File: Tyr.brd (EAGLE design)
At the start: 152.4 x 115.6 mm, 206 parts, among them J1 TYR_TYR_DISPLAY, Q1 DTC123J, SW1 BUTTON, U1 MCP1700T, U2 CONTROLLER_PRTR5V0U2X, U3 STM32F303CC, U4 MB85RC256V, U6 TYR_TPS2552, X1 CONTROLLER_USB-C-12PUSB-C-12P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, Y1 8Mhz

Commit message: Y branching
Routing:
- net 3.3V: track 397.3 -> 396.4 mm
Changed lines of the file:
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@@
 <wire x1="146.0921875" y1="69.74125" x2="145.4071875" y2="69.05625" width="0.3048" layer="16"/>
 <wire x1="151.209375" y1="31.5515625" x2="149.4234375" y2="31.5515625" width="0.3048" layer="16"/>
-<wire x1="149.4234375" y1="31.5515625" x2="147.6375" y2="31.5515625" width="0.3048" layer="16"/>
-<wire x1="147.6375" y1="31.5515625" x2="145.8515625" y2="31.5515625" width="0.3048" layer="16"/>
-<wire x1="145.8515625" y1="31.5515625" x2="144.065625" y2="31.5515625" width="0.3048" layer="16"/>
-<wire x1="144.065625" y1="31.5515625" x2="142.2796875" y2="31.5515625" width="0.3048" layer="16"/>
-<wire x1="142.2796875" y1="31.5515625" x2="140.49375" y2="31.5515625" width="0.3048" layer="16"/>
+<wire x1="148.828125" y1="31.5515625" x2="147.6375" y2="31.5515625" width="0.3048" layer="16"/>
+<wire x1="147.0421875" y1="31.5515625" x2="145.8515625" y2="31.5515625" width="0.3048" layer="16"/>
+<wire x1="145.25625" y1="31.5515625" x2="144.065625" y2="31.5515625" width="0.3048" layer="16"/>
+<wire x1="143.4703125" y1="31.5515625" x2="142.2796875" y2="31.5515625" width="0.3048" layer="16"/>
+<wire x1="141.684375" y1="31.5515625" x2="140.49375" y2="31.5515625" width="0.3048" layer="16"/>
 <wire x1="140.49375" y1="31.5515625" x2="140.19609375" y2="31.25390625" width="0.3048" layer="16"/>
 <wire x1="140.19609375" y1="31.25390625" x2="140.19609375" y2="30.6765625" width="0.3048" layer="16"/>
-<wire x1="141.98203125" y1="30.6765625" x2="141.98203125" y2="31.25390625" width="0.3048" layer="16"/>
 <wire x1="141.98203125" y1="31.25390625" x2="142.2796875" y2="31.5515625" width="0.3048" layer="16"/>
-<wire x1="143.76796875" y1="30.6765625" x2="143.76796875" y2="31.25390625" width="0.3048" layer="16"/>
 <wire x1="143.76796875" y1="31.25390625" x2="144.065625" y2="31.5515625" width="0.3048" layer="16"/>
-<wire x1="145.55390625" y1="30.6765625" x2="145.55390625" y2="31.25390625" width="0.3048" layer="16"/>
 <wire x1="145.55390625" y1="31.25390625" x2="145.8515625" y2="31.5515625" width="0.3048" layer="16"/>
-<wire x1="147.33984375" y1="30.6765625" x2="147.33984375" y2="31.25390625" width="0.3048" layer="16"/>
 <wire x1="147.33984375" y1="31.25390625" x2="147.6375" y2="31.5515625" width="0.3048" layer="16"/>
-<wire x1="149.12578125" y1="30.6765625" x2="149.12578125" y2="31.25390625" width="0.3048" layer="16"/>
 <wire x1="149.12578125" y1="31.25390625" x2="149.4234375" y2="31.5515625" width="0.3048" layer="16"/>
 <wire x1="147.33984375" y1="30.6765625" x2="149.12578125" y2="30.6765625" width="0.3048" layer="16"/>
@@
 <wire x1="118.4671875" y1="7.7390625" x2="115.8875" y2="10.31875" width="0.1524" layer="1"/>
 <wire x1="115.8875" y1="10.31875" x2="115.8875" y2="10.4775" width="0.1524" layer="1"/>
+<wire x1="148.828125" y1="31.5515625" x2="149.12578125" y2="31.25390625" width="0.3048" layer="16"/>
+<wire x1="149.12578125" y1="31.25390625" x2="149.12578125" y2="30.6765625" width="0.3048" layer="16"/>
+<wire x1="147.0421875" y1="31.5515625" x2="147.33984375" y2="31.25390625" width="0.3048" layer="16"/>
+<wire x1="147.33984375" y1="31.25390625" x2="147.33984375" y2="30.6765625" width="0.3048" layer="16"/>
+<wire x1="145.25625" y1="31.5515625" x2="145.55390625" y2="31.25390625" width="0.3048" layer="16"/>
+<wire x1="145.55390625" y1="31.25390625" x2="145.55390625" y2="30.6765625" width="0.3048" layer="16"/>
+<wire x1="143.4703125" y1="31.5515625" x2="143.76796875" y2="31.25390625" width="0.3048" layer="16"/>
+<wire x1="143.76796875" y1="31.25390625" x2="143.76796875" y2="30.6765625" width="0.3048" layer="16"/>
+<wire x1="141.684375" y1="31.5515625" x2="141.98203125" y2="31.25390625" width="0.3048" layer="16"/>
+<wire x1="141.98203125" y1="31.25390625" x2="141.98203125" y2="30.6765625" width="0.3048" layer="16"/>
 </signal>
 <signal name="NRST">

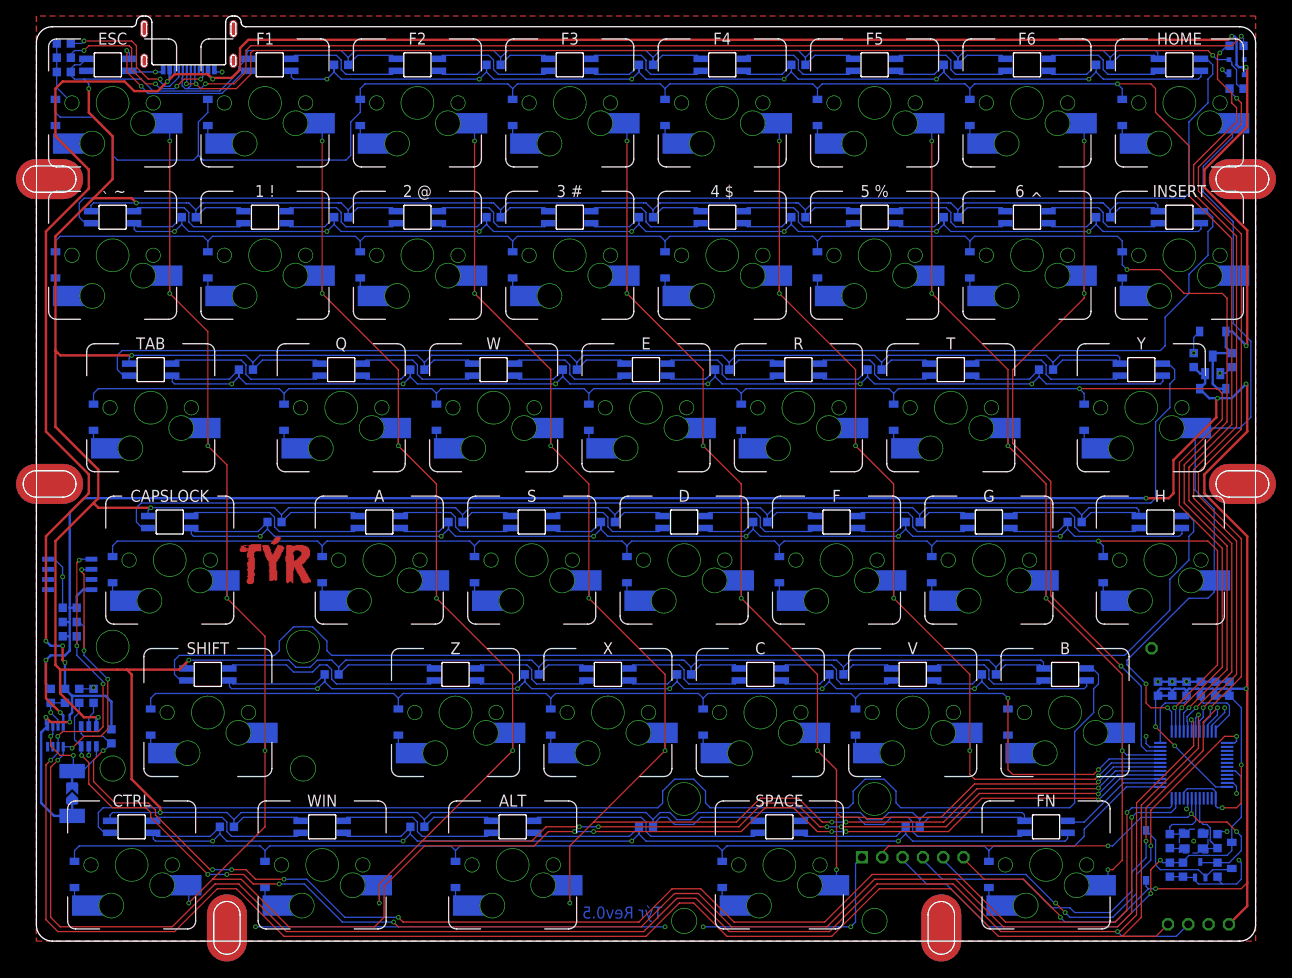
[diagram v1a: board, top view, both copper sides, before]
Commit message: Ground plane under STM32
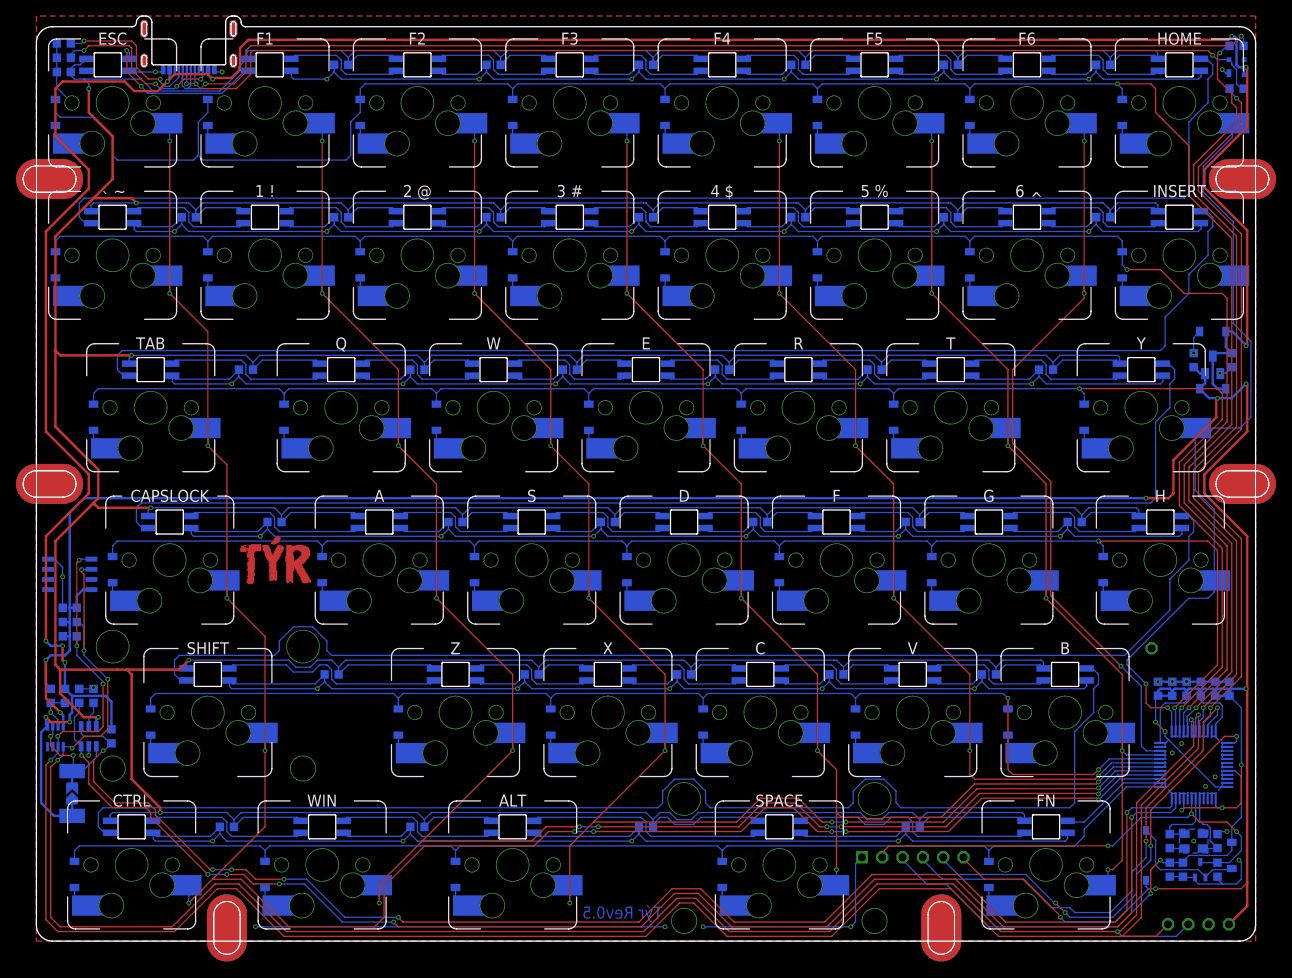
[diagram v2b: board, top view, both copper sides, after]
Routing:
- net GND: track 1189.0 -> 1175.5 mm
- net 3.3V: track 396.4 -> 396.0 mm, vias 12 -> 13

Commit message: Y branching
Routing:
- net LED_VCC: track 1250.6 -> 1226.3 mm

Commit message: Update logo
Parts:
- added U$1: LOGO_TYR, Tyr:LOGO_TYR_COPPER
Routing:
- net GND: track 1175.5 -> 1177.3 mm, vias 57 -> 59
- net COLUMN7: track 108.6 -> 107.8 mm
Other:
- board text added: "C:/Users/Brian/Desktop/TYR STOP.bmp"
- board text added: "C:/Users/Brian/Desktop/TYR TEXT.bmp"
- board text removed: "C:/Users/Brian/Desktop/Tyr V4.bmp"
- board text removed: "D:/Users/Brian/Pictures/Tyr.bmp"

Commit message: Update
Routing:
- net COLUMN7: track 107.8 -> 101.0 mm
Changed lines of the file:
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@@
 <text x="105.7275" y="8.5725" size="1" layer="22" font="vector" ratio="13" rot="MR315" align="center-left">NRST</text>
 <text x="103.1875" y="12.7" size="1" layer="22" font="vector" ratio="13" rot="MR0" align="center">GND</text>
-<text x="73.2234375" y="3.571875" size="1.5" layer="16" font="vector" ratio="13" rot="MR0" align="center">Týr Rev0.5</text>
-<text x="73.2234375" y="3.571875" size="1.5" layer="30" font="vector" ratio="13" rot="MR0" align="center">Týr Rev0.5</text>
+<text x="76.2" y="7.14375" size="1.5" layer="16" font="vector" ratio="13" rot="MR0" align="center">Týr Rev0.5</text>
+<text x="76.2" y="7.14375" size="1.5" layer="30" font="vector" ratio="13" rot="MR0" align="center">Týr Rev0.5</text>
 <text x="0" y="-0.5" size="0.2" layer="200" font="vector">C:/Users/Brian/Desktop/TYR TEXT.bmp</text>
 <text x="0" y="-0.5" size="0.2" layer="225" font="vector">C:/Users/Brian/Desktop/TYR STOP.bmp</text>
@@
 <contactref element="KEYSWITCH30" pad="P$1"/>
 <contactref element="KEYSWITCH23" pad="P$1"/>
-<wire x1="144.065625" y1="42.8625" x2="136.3265625" y2="35.1234375" width="0.1524" layer="16"/>
 <wire x1="145.8515625" y1="96.8446875" x2="145.8515625" y2="93.6553125" width="0.1524" layer="16"/>
 <wire x1="145.8515625" y1="93.6553125" x2="149.61" y2="89.896875" width="0.1524" layer="16"/>
@@
 <contactref element="KEYSWITCH30" pad="HOLE3"/>
 <wire x1="149.5190625" y1="100.5121875" x2="145.8515625" y2="96.8446875" width="0.1524" layer="16"/>
-<wire x1="144.065625" y1="42.8625" x2="146.446875" y2="42.8625" width="0.1524" layer="16"/>
-<wire x1="146.446875" y1="42.8625" x2="147.22875" y2="43.644375" width="0.1524" layer="16"/>
-<wire x1="147.22875" y1="43.644375" x2="147.22875" y2="45.085" width="0.1524" layer="16"/>
+<wire x1="147.0421875" y1="42.8625" x2="147.22875" y2="43.0490625" width="0.1524" layer="16"/>
+<wire x1="147.22875" y1="43.0490625" x2="147.22875" y2="45.085" width="0.1524" layer="16"/>
 <wire x1="149.5190625" y1="100.5121875" x2="149.5190625" y2="102.1440625" width="0.1524" layer="16"/>
 <wire x1="149.5190625" y1="102.1440625" x2="149.61" y2="102.235" width="0.1524" layer="16"/>
@@
 <wire x1="141.9109375" y1="26.2048625" x2="141.9109375" y2="28.64609375" width="0.1524" layer="16"/>
 <via x="141.38671875" y="29.1703125" extent="1-16" drill="0.35"/>
-<wire x1="141.38671875" y1="29.1703125" x2="139.303125" y2="29.1703125" width="0.1524" layer="1"/>
-<wire x1="139.303125" y1="29.1703125" x2="138.7078125" y2="29.765625" width="0.1524" layer="1"/>
-<wire x1="138.7078125" y1="29.765625" x2="138.7078125" y2="32.146875" width="0.1524" layer="1"/>
-<via x="138.7078125" y="32.146875" extent="1-16" drill="0.35"/>
-<wire x1="136.3265625" y1="35.1234375" x2="136.3265625" y2="34.528125" width="0.1524" layer="16"/>
-<wire x1="136.3265625" y1="34.528125" x2="138.7078125" y2="32.146875" width="0.1524" layer="16"/>
+<wire x1="141.38671875" y1="29.1703125" x2="147.0421875" y2="34.82578125" width="0.1524" layer="1"/>
+<wire x1="147.0421875" y1="34.82578125" x2="147.0421875" y2="42.8625" width="0.1524" layer="1"/>
+<via x="147.0421875" y="42.8625" extent="1-16" drill="0.35"/>
 </signal>
 <signal name="COLUMN6">
@@
 <wire x1="151.209375" y1="69.6515625" x2="149.4234375" y2="67.865625" width="0.3048" layer="16"/>
 <via x="151.209375" y="69.6515625" extent="1-16" drill="0.35"/>
-<via x="151.209375" y="31.5515625" extent="1-16" drill="0.35"/>
 <contactref element="J1" pad="VIN"/>
-<wire x1="151.358203125" y1="4.391953125" x2="151.358203125" y2="7.14375" width="0.3048" layer="1"/>
-<wire x1="151.358203125" y1="7.14375" x2="151.358203125" y2="7.292578125" width="0.3048" layer="1"/>
+<wire x1="151.358203125" y1="4.391953125" x2="151.358203125" y2="7.292578125" width="0.3048" layer="1"/>
 <wire x1="151.358203125" y1="4.391953125" x2="149.06625" y2="2.1" width="0.3048" layer="1"/>
 <via x="139.8984375" y="6.5484375" extent="1-16" drill="0.35"/>
 <wire x1="139.8984375" y1="6.5484375" x2="150.6140625" y2="6.5484375" width="0.1524" layer="1"/>
-<wire x1="151.358203125" y1="7.292578125" x2="151.209375" y2="7.14375" width="0.1524" layer="1"/>
 <contactref element="SW1" pad="P$2"/>
-<wire x1="151.209375" y1="7.14375" x2="150.6140625" y2="6.5484375" width="0.1524" layer="1"/>
+<wire x1="151.358203125" y1="7.292578125" x2="150.6140625" y2="6.5484375" width="0.1524" layer="1"/>
 <wire x1="139.8984375" y1="6.5484375" x2="139.005078125" y2="6.5484375" width="0.1524" layer="16"/>
 <contactref element="PH1" pad="6"/>
@@
 <wire x1="146.0921875" y1="70.9328125" x2="146.0921875" y2="69.74125" width="0.3048" layer="16"/>
 <wire x1="146.0921875" y1="69.74125" x2="145.4071875" y2="69.05625" width="0.3048" layer="16"/>
-<wire x1="151.209375" y1="31.5515625" x2="149.4234375" y2="31.5515625" width="0.3048" layer="16"/>
 <wire x1="148.828125" y1="31.5515625" x2="147.6375" y2="31.5515625" width="0.3048" layer="16"/>
 <wire x1="147.0421875" y1="31.5515625" x2="145.8515625" y2="31.5515625" width="0.3048" layer="16"/>
@@
 <wire x1="5.0421875" y1="43.1421875" x2="5.0421875" y2="41.671875" width="0.3048" layer="16"/>
 <wire x1="5.8340625" y1="43.9340625" x2="5.0421875" y2="43.1421875" width="0.3048" layer="16"/>
-<wire x1="151.358203125" y1="31.5515625" x2="151.358203125" y2="7.292578125" width="0.3048" layer="1"/>
-<wire x1="151.358203125" y1="31.5515625" x2="151.358203125" y2="50.6015625" width="0.3048" layer="1"/>
-<wire x1="151.209375" y1="31.5515625" x2="151.358203125" y2="31.5515625" width="0.3048" layer="1"/>
+<wire x1="151.358203125" y1="50.6015625" x2="151.358203125" y2="32.146875" width="0.3048" layer="1"/>
+<wire x1="151.358203125" y1="30.95625" x2="151.358203125" y2="7.292578125" width="0.3048" layer="1"/>
 <wire x1="118.4671875" y1="7.7390625" x2="115.8875" y2="10.31875" width="0.1524" layer="1"/>
 <wire x1="115.8875" y1="10.31875" x2="115.8875" y2="10.4775" width="0.1524" layer="1"/>
@@
 <wire x1="141.0890625" y1="25.5984375" x2="141.0890625" y2="26.19375" width="0.1524" layer="16"/>
 <wire x1="147.4109375" y1="19.2765625" x2="141.0890625" y2="25.5984375" width="0.1524" layer="16"/>
-<wire x1="151.209375" y1="7.14375" x2="151.209375" y2="7.14375" width="0.1524" layer="1"/>
+<wire x1="149.4234375" y1="31.5515625" x2="150.6140625" y2="31.5515625" width="0.3048" layer="16"/>
+<via x="150.6140625" y="31.5515625" extent="1-16" drill="0.35"/>
+<wire x1="151.358203125" y1="32.146875" x2="150.762890625" y2="31.5515625" width="0.3048" layer="1"/>
+<wire x1="151.358203125" y1="30.95625" x2="150.762890625" y2="31.5515625" width="0.3048" layer="1"/>
+<wire x1="150.762890625" y1="31.5515625" x2="150.6140625" y2="31.5515625" width="0.3048" layer="1"/>
 </signal>
 <signal name="NRST">

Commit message: Update Tyr.brd
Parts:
- moved R11 0.60 mm to (4.46, 17.9)
- moved SJ1 0.60 mm to (4.46, 17.9)
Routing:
- net N$53: track 154.6 -> 147.8 mm, vias 0 -> 4
- net N$59: track 149.0 -> 145.9 mm, vias 0 -> 2
- net COLUMN6: track 99.2 -> 100.3 mm
- net N$2: track 14.9 -> 15.9 mm
- net COLUMN0: track 269.7 -> 270.7 mm
- net COLUMN1: track 242.3 -> 243.3 mm
- net VCC: track 335.0 -> 336.0 mm
- net COLUMN2: track 218.1 -> 219.0 mm
- net LED_VCC: track 1226.3 -> 1227.0 mm
- net COLUMN7: track 101.0 -> 100.4 mm

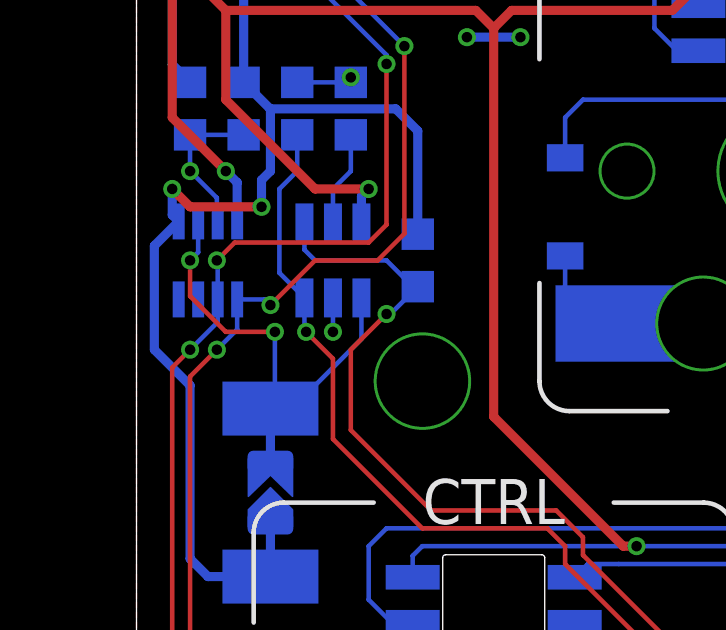
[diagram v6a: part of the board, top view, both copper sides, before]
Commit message: Update trace width
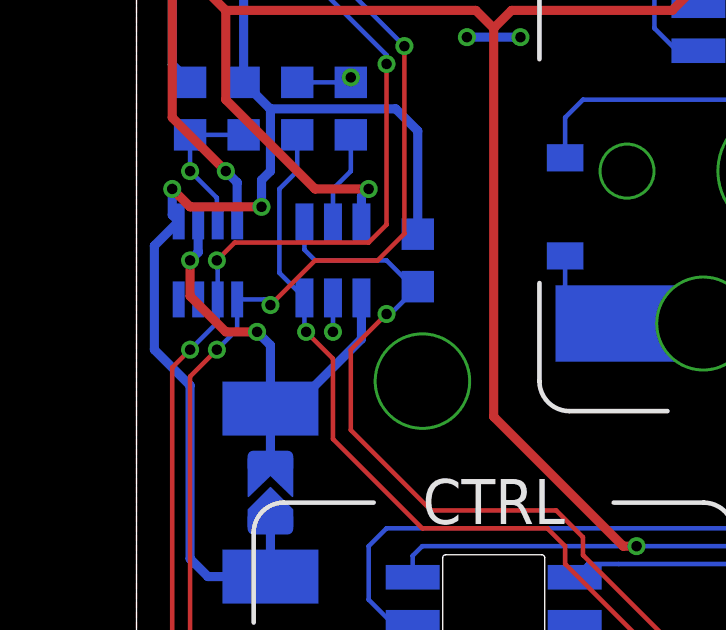
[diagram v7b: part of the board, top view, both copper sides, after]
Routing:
- net N$2: track 15.9 -> 15.2 mm
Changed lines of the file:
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@@
 <contactref element="SJ1" pad="2"/>
 <wire x1="4.46484375" y1="20.659375" x2="4.46484375" y2="18.875375" width="0.3048" layer="16"/>
-<wire x1="4.7625" y1="21.2546875" x2="4.46484375" y2="20.95703125" width="0.3048" layer="16"/>
-<wire x1="4.46484375" y1="20.95703125" x2="4.46484375" y2="20.659375" width="0.3048" layer="16"/>
-<wire x1="7.4984375" y1="24.3484375" x2="7.4984375" y2="22.9765625" width="0.1524" layer="16"/>
-<wire x1="5.7765625" y1="21.2546875" x2="4.7625" y2="21.2546875" width="0.1524" layer="16"/>
-<wire x1="7.4984375" y1="22.9765625" x2="5.7765625" y2="21.2546875" width="0.1524" layer="16"/>
-<via x="4.613671875" y="23.2171875" extent="1-16" drill="0.35"/>
-<wire x1="4.613671875" y1="23.2171875" x2="4.6136625" y2="20.808190625" width="0.1524" layer="16"/>
-<wire x1="4.46484375" y1="20.659375" x2="4.6136625" y2="20.808190625" width="0.1524" layer="16"/>
+<via x="4.018359375" y="23.2171875" extent="1-16" drill="0.35"/>
 <via x="1.7859375" y="25.5984375" extent="1-16" drill="0.35"/>
-<wire x1="1.7859375" y1="25.5984375" x2="2.05625" y2="25.86875" width="0.1524" layer="16"/>
-<wire x1="2.05625" y1="25.86875" x2="2.05625" y2="26.8984375" width="0.1524" layer="16"/>
-<wire x1="4.613671875" y1="23.2171875" x2="2.97656875" y2="23.21718125" width="0.1524" layer="1"/>
-<wire x1="1.7859375" y1="24.4078125" x2="1.7859375" y2="25.5984375" width="0.1524" layer="1"/>
-<wire x1="2.97656875" y1="23.21718125" x2="1.7859375" y2="24.4078125" width="0.1524" layer="1"/>
+<wire x1="4.46484375" y1="20.659375" x2="4.46484375" y2="22.770703125" width="0.3048" layer="16"/>
+<wire x1="4.46484375" y1="22.770703125" x2="4.018359375" y2="23.2171875" width="0.3048" layer="16"/>
+<wire x1="4.018359375" y1="23.2171875" x2="2.9765625" y2="23.2171875" width="0.3048" layer="1"/>
+<wire x1="2.9765625" y1="23.2171875" x2="1.7859375" y2="24.4078125" width="0.3048" layer="1"/>
+<wire x1="1.7859375" y1="24.4078125" x2="1.7859375" y2="25.5984375" width="0.3048" layer="1"/>
+<wire x1="2.05625" y1="26.8984375" x2="2.05625" y2="25.86875" width="0.3048" layer="16"/>
+<wire x1="2.05625" y1="25.86875" x2="1.7859375" y2="25.5984375" width="0.3048" layer="16"/>
+<wire x1="7.4984375" y1="24.3484375" x2="7.4984375" y2="22.9765625" width="0.3048" layer="16"/>
+<wire x1="5.18125" y1="20.659375" x2="4.46484375" y2="20.659375" width="0.3048" layer="16"/>
+<wire x1="7.4984375" y1="22.9765625" x2="5.18125" y2="20.659375" width="0.3048" layer="16"/>
 </signal>
 <signal name="LED_DATA">
